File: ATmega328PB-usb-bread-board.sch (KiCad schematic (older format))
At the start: 37 parts, among them J1 Conn_01x17, J2 Conn_01x17, J3 USB_B_Micro, J4 AVR-ISP-6, J5 Grove-I2C-connector, J6 Grove-I2C-connector, J7 Grove-I2C-connector, U1 ATmega328PB-MU, U2 CP2102N-A01-GQFN28, U3 LMV358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

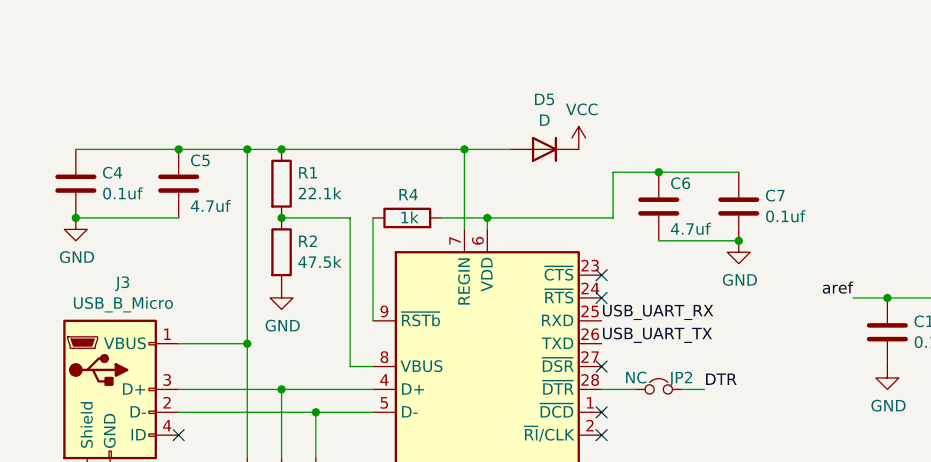
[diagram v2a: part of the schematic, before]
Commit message: Supply 3V3 to cp2102
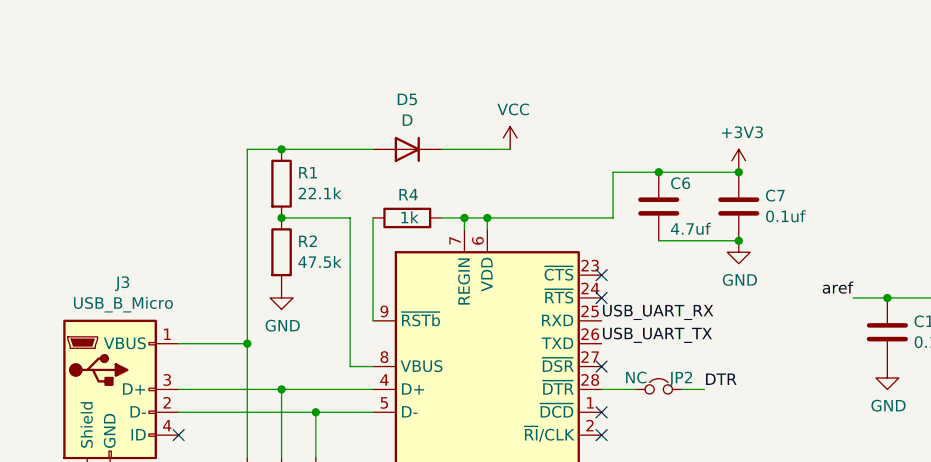
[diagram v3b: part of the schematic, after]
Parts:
- removed C4: 0.1uf, Capacitor_SMD:C_0603_1608Metric, symbol Device:C
- removed C5: 4.7uf, Capacitor_SMD:C_0402_1005Metric, symbol Device:C
- JP1, JP2, JP3, JP4: footprint Jumper:SolderJumper-2_P1.3mm_Bridged_RoundedPad1.0x1.5mm -> my-kicad-footprints:SolderJumper-2_P1.3mm_Bridged_RoundedPad1.0x1.5mm
- U5: footprint (none) -> Package_TO_SOT_SMD:SOT-23-5
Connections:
- net +3V3: now also C6.1, C7.1, R4.2, U2.6 (VDD), U2.7 (REGIN)
- net at D1.1 (K), D5.2 (A), J3.1 (VBUS)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: no longer U2.7 (REGIN)
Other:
- moved on the sheet: D5
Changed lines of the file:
@@
 F 0 "JP1" H 5650 1712 50  0000 C CNN
 F 1 "NC" H 5650 1621 50  0000 C CNN
-F 2 "Jumper:SolderJumper-2_P1.3mm_Bridged_RoundedPad1.0x1.5mm" H 5650 1500 50  0001 C CNN
+F 2 "my-kicad-footprints:SolderJumper-2_P1.3mm_Bridged_RoundedPad1.0x1.5mm" H 5650 1500 50  0001 C CNN
 F 3 "~" H 5650 1500 50  0001 C CNN
 	1    5650 1500
@@
 	1900 1400 2050 1400
 Connection ~ 1900 2250
-Wire Wire Line
-	2050 1400 2850 1400
-Wire Wire Line
-	2850 1400 2850 1750
-Connection ~ 2050 1400
 Connection ~ 2050 1700
 Wire Wire Line
@@
 F 0 "JP4" H 6600 3900 50  0000 C CNN
 F 1 "NC" H 6400 3900 50  0000 C CNN
-F 2 "Jumper:SolderJumper-2_P1.3mm_Bridged_RoundedPad1.0x1.5mm" H 6500 3850 50  0001 C CNN
+F 2 "my-kicad-footprints:SolderJumper-2_P1.3mm_Bridged_RoundedPad1.0x1.5mm" H 6500 3850 50  0001 C CNN
 F 3 "~" H 6500 3850 50  0001 C CNN
 	1    6500 3850
@@
 F 0 "JP3" H 6600 3800 50  0000 C CNN
 F 1 "NC" H 6400 3800 50  0000 C CNN
-F 2 "Jumper:SolderJumper-2_P1.3mm_Bridged_RoundedPad1.0x1.5mm" H 6500 3750 50  0001 C CNN
+F 2 "my-kicad-footprints:SolderJumper-2_P1.3mm_Bridged_RoundedPad1.0x1.5mm" H 6500 3750 50  0001 C CNN
 F 3 "~" H 6500 3750 50  0001 C CNN
 	1    6500 3750
@@
 F 0 "JP2" H 3800 2500 50  0000 C CNN
 F 1 "NC" H 3600 2500 50  0000 C CNN
-F 2 "Jumper:SolderJumper-2_P1.3mm_Bridged_RoundedPad1.0x1.5mm" H 3700 2450 50  0001 C CNN
+F 2 "my-kicad-footprints:SolderJumper-2_P1.3mm_Bridged_RoundedPad1.0x1.5mm" H 3700 2450 50  0001 C CNN
 F 3 "~" H 3700 2450 50  0001 C CNN
 	1    3700 2450
@@
 L Device:D D5
 U 1 1 5F87D197
-P 3200 1400
-F 0 "D5" H 3200 1183 50  0000 C CNN
-F 1 "D" H 3200 1274 50  0000 C CNN
-F 2 "Diode_SMD:D_SOD-123F" H 3200 1400 50  0001 C CNN
-F 3 "~" H 3200 1400 50  0001 C CNN
-	1    3200 1400
+P 2600 1400
+F 0 "D5" H 2600 1183 50  0000 C CNN
+F 1 "D" H 2600 1274 50  0000 C CNN
+F 2 "Diode_SMD:D_SOD-123F" H 2600 1400 50  0001 C CNN
+F 3 "~" H 2600 1400 50  0001 C CNN
+	1    2600 1400
 	-1   0    0    1
 $EndComp
@@
 L power:VCC #PWR0123
 U 1 1 5F87D6DB
-P 3350 1400
-F 0 "#PWR0123" H 3350 1250 50  0001 C CNN
-F 1 "VCC" H 3365 1573 50  0000 C CNN
-F 2 "" H 3350 1400 50  0001 C CNN
-F 3 "" H 3350 1400 50  0001 C CNN
-	1    3350 1400
-	1    0    0    -1
-$EndComp
-Connection ~ 2850 1400
-$Comp
-L my-kicad-symbols:NJM12888F33 U4
-U 1 1 5F8C64C1
-P 9850 1800
-F 0 "U4" H 10000 2250 50  0000 C CNN
-F 1 "NJM12888F33" H 10150 2100 50  0000 C CNN
-F 2 "Package_TO_SOT_SMD:SOT-23-5" H 9850 1800 50  0001 C CNN
-F 3 "" H 9850 1800 50  0001 C CNN
-	1    9850 1800
-	1    0    0    -1
-$EndComp
-$Comp
-L power:VCC #PWR0111
-U 1 1 5F8C761A
-P 9200 1500
-F 0 "#PWR0111" H 9200 1350 50  0001 C CNN
-F 1 "VCC" H 9215 1673 50  0000 C CNN
-F 2 "" H 9200 1500 50  0001 C CNN
-F 3 "" H 9200 1500 50  0001 C CNN
-	1    9200 1500
-	1    0    0    -1
-$EndComp
-$Comp
-L power:GND #PWR0124
-U 1 1 5F8C7AD0
-P 9200 2200
-F 0 "#PWR0124" H 9200 1950 50  0001 C CNN
-F 1 "GND" H 9205 2027 50  0000 C CNN
-F 2 "" H 9200 2200 50  0001 C CNN
-F 3 "" H 9200 2200 50  0001 C CNN
-	1    9200 2200
-	1    0    0    -1
-$EndComp
-$Comp
-L Device:C C8
-U 1 1 5F8C87B4
-P 9200 1800
-F 0 "C8" H 9250 1900 50  0000 L CNN
-F 1 "0.1uf" H 9250 1650 50  0000 L CNN
-F 2 "Capacitor_SMD:C_0603_1608Metric" H 9238 1650 50  0001 C CNN
-F 3 "~" H 9200 1800 50  0001 C CNN
-	1    9200 1800
-	1    0    0    -1
-$EndComp
-Wire Wire Line
-	9200 1500 9450 1500
-Wire Wire Line
-	9450 1500 9450 1800
-Connection ~ 9450 1500
-Wire Wire Line
-	9450 1500 9850 1500
-Wire Wire Line
-	9200 1650 9200 1500
-Connection ~ 9200 1500
-$Comp
-L Device:C C10
-U 1 1 5F8D0B51
-P 10250 2050
-F 0 "C10" H 10300 2150 50  0000 L CNN
-F 1 "10nf" H 10300 1950 50  0000 L CNN
-F 2 "Capacitor_SMD:C_0603_1608Metric" H 10288 1900 50  0001 C CNN
-F 3 "~" H 10250 2050 50  0001 C CNN
-	1    10250 2050
-	1    0    0    -1
-$EndComp
-Wire Wire Line
-	9200 1950 9200 2200
-Wire Wire Line
-	9200 2200 9850 2200
-Connection ~ 9200 2200
-Wire Wire Line
-	9850 2200 9850 2100
-Connection ~ 9850 2200
-Wire Wire Line
-	9850 2200 10250 2200
-$Comp
-L Device:C C12
-U 1 1 5F8D5F68
-P 10600 1950
-F 0 "C12" H 10650 2050 50  0000 L CNN
-F 1 "4.7uf" H 10650 1850 50  0000 L CNN
-F 2 "Capacitor_SMD:C_0402_1005Metric" H 10638 1800 50  0001 C CNN
-F 3 "~" H 10600 1950 50  0001 C CNN
-	1    10600 1950
-	1    0    0    -1
-$EndComp
-$Comp
-L power:+3V3 #PWR0125
-U 1 1 5F8D6BD8
-P 10600 1700
-F 0 "#PWR0125" H 10600 1550 50  0001 C CNN
-F 1 "+3V3" H 10615 1873 50  0000 C CNN
-F 2 "" H 10600 1700 50  0001 C CNN
-F 3 "" H 10600 1700 50  0001 C CNN
-	1    10600 1700
-	1    0    0    -1
-$EndComp
-Wire Wire Line
-	10600 1700 10600 1800
-Wire Wire Line
-	10600 1700 10250 1700
-Connection ~ 10600 1700
-Wire Wire Line
-	10250 2200 10600 2200
-Wire Wire Line
-	10600 2200 10600 2100
-Connection ~ 10250 2200
+P 3050 1400
+F 0 "#PWR0123" H 3050 1250 50  0001 C CNN
+F 1 "VCC" H 3065 1573 50  0000 C CNN
+F 2 "" H 3050 1400 50  0001 C CNN
+F 3 "" H 3050 1400 50  0001 C CNN
+	1    3050 1400
+	1    0    0    -1
+$EndComp
 $Comp
 L power:+3V3 #PWR0126
@@
 F 0 "U5" H 9950 3950 50  0000 L CNN
 F 1 "SiT2001B-MEMS-Clock-Generator" H 9600 3850 50  0000 L CNN
-F 2 "" H 10000 3350 50  0001 C CNN
+F 2 "Package_TO_SOT_SMD:SOT-23-5" H 10000 3350 50  0001 C CNN
 F 3 "" H 10000 3350 50  0001 C CNN
 	1    10000 3350
@@
 16MHz
 NoConn ~ 9600 3350
-Wire Wire Line
-	2850 1400 3050 1400
 $Comp
 L Device:R R4
@@
 	2450 1700 2450 2150
 Wire Wire Line
-	2750 1700 2950 1700
+	2750 1700 2850 1700
 Wire Wire Line
 	2950 1700 2950 1750
-$Comp
-L Device:C C5
-U 1 1 5F8FC33B
-P 1600 1550
-F 0 "C5" H 1650 1650 50  0000 L CNN
-F 1 "4.7uf" H 1650 1450 50  0000 L CNN
-F 2 "Capacitor_SMD:C_0402_1005Metric" H 1638 1400 50  0001 C CNN
-F 3 "~" H 1600 1550 50  0001 C CNN
-	1    1600 1550
-	1    0    0    -1
-$EndComp
-$Comp
-L Device:C C4
-U 1 1 5F9005EE
-P 1150 1550
-F 0 "C4" H 1265 1596 50  0000 L CNN
-F 1 "0.1uf" H 1265 1505 50  0000 L CNN
-F 2 "Capacitor_SMD:C_0603_1608Metric" H 1188 1400 50  0001 C CNN
-F 3 "~" H 1150 1550 50  0001 C CNN
-	1    1150 1550
-	1    0    0    -1
-$EndComp
-$Comp
-L power:GND #PWR0129
-U 1 1 5F9017BB
-P 1150 1700
-F 0 "#PWR0129" H 1150 1450 50  0001 C CNN
-F 1 "GND" H 1155 1527 50  0000 C CNN
-F 2 "" H 1150 1700 50  0001 C CNN
-F 3 "" H 1150 1700 50  0001 C CNN
-	1    1150 1700
-	1    0    0    -1
-$EndComp
-Wire Wire Line
-	1150 1700 1600 1700
-Connection ~ 1150 1700
-Wire Wire Line
-	1900 1400 1600 1400
-Connection ~ 1900 1400
-Connection ~ 1600 1400
-Wire Wire Line
-	1600 1400 1150 1400
 $Comp
 L Device:C C6
@@
 Wire Wire Line
 	3700 1500 4050 1500
+Wire Wire Line
+	2050 1400 2450 1400
+Connection ~ 2050 1400
+$Comp
+L power:+3V3 #PWR?
+U 1 1 5F92FD3C
+P 4050 1500
+F 0 "#PWR?" H 4050 1350 50  0001 C CNN
+F 1 "+3V3" H 4065 1673 50  0000 C CNN
+F 2 "" H 4050 1500 50  0001 C CNN
+F 3 "" H 4050 1500 50  0001 C CNN
+	1    4050 1500
+	1    0    0    -1
+$EndComp
+Connection ~ 4050 1500
+Wire Wire Line
+	10600 2200 10600 2100
+Wire Wire Line
+	10600 1700 10250 1700
+Wire Wire Line
+	10600 1700 10600 1800
+Connection ~ 10600 1700
+$Comp
+L power:+3V3 #PWR0125
+U 1 1 5F8D6BD8
+P 10600 1700
+F 0 "#PWR0125" H 10600 1550 50  0001 C CNN
+F 1 "+3V3" H 10615 1873 50  0000 C CNN
+F 2 "" H 10600 1700 50  0001 C CNN
+F 3 "" H 10600 1700 50  0001 C CNN
+	1    10600 1700
+	1    0    0    -1
+$EndComp
+$Comp
+L Device:C C12
+U 1 1 5F8D5F68
+P 10600 1950
+F 0 "C12" H 10650 2050 50  0000 L CNN
+F 1 "4.7uf" H 10650 1850 50  0000 L CNN
+F 2 "Capacitor_SMD:C_0402_1005Metric" H 10638 1800 50  0001 C CNN
+F 3 "~" H 10600 1950 50  0001 C CNN
+	1    10600 1950
+	1    0    0    -1
+$EndComp
+Wire Wire Line
+	9850 2200 9850 2100
+Connection ~ 9850 2200
+Wire Wire Line
+	9200 2200 9850 2200
+Wire Wire Line
+	9200 1950 9200 2200
+Wire Wire Line
+	10250 2200 10600 2200
+Wire Wire Line
+	9850 2200 10250 2200
+Connection ~ 10250 2200
+$Comp
+L Device:C C10
+U 1 1 5F8D0B51
+P 10250 2050
+F 0 "C10" H 10300 2150 50  0000 L CNN
+F 1 "10nf" H 10300 1950 50  0000 L CNN
+F 2 "Capacitor_SMD:C_0603_1608Metric" H 10288 1900 50  0001 C CNN
+F 3 "~" H 10250 2050 50  0001 C CNN
+	1    10250 2050
+	1    0    0    -1
+$EndComp
+Wire Wire Line
+	9200 1650 9200 1500
+Wire Wire Line
+	9450 1500 9850 1500
+Wire Wire Line
+	9450 1500 9450 1800
+Connection ~ 9450 1500
+Wire Wire Line
+	9200 1500 9450 1500
+$Comp
+L Device:C C8
+U 1 1 5F8C87B4
+P 9200 1800
+F 0 "C8" H 9250 1900 50  0000 L CNN
+F 1 "0.1uf" H 9250 1650 50  0000 L CNN
+F 2 "Capacitor_SMD:C_0603_1608Metric" H 9238 1650 50  0001 C CNN
+F 3 "~" H 9200 1800 50  0001 C CNN
+	1    9200 1800
+	1    0    0    -1
+$EndComp
+Connection ~ 9200 2200
+$Comp
+L power:GND #PWR0124
+U 1 1 5F8C7AD0
+P 9200 2200
+F 0 "#PWR0124" H 9200 1950 50  0001 C CNN
+F 1 "GND" H 9205 2027 50  0000 C CNN
+F 2 "" H 9200 2200 50  0001 C CNN
+F 3 "" H 9200 2200 50  0001 C CNN
+	1    9200 2200
+	1    0    0    -1
+$EndComp
+Connection ~ 9200 1500
+$Comp
+L power:VCC #PWR0111
+U 1 1 5F8C761A
+P 9200 1500
+F 0 "#PWR0111" H 9200 1350 50  0001 C CNN
+F 1 "VCC" H 9215 1673 50  0000 C CNN
+F 2 "" H 9200 1500 50  0001 C CNN
+F 3 "" H 9200 1500 50  0001 C CNN
+	1    9200 1500
+	1    0    0    -1
+$EndComp
+$Comp
+L my-kicad-symbols:NJM12888F33 U4
+U 1 1 5F8C64C1
+P 9850 1800
+F 0 "U4" H 10000 2250 50  0000 C CNN
+F 1 "NJM12888F33" H 10150 2100 50  0000 C CNN
+F 2 "Package_TO_SOT_SMD:SOT-23-5" H 9850 1800 50  0001 C CNN
+F 3 "" H 9850 1800 50  0001 C CNN
+	1    9850 1800
+	1    0    0    -1
+$EndComp
+Wire Wire Line
+	2750 1400 3050 1400
+Wire Wire Line
+	2850 1700 2850 1750
+Connection ~ 2850 1700
+Wire Wire Line
+	2850 1700 2950 1700
 $EndSCHEMATC

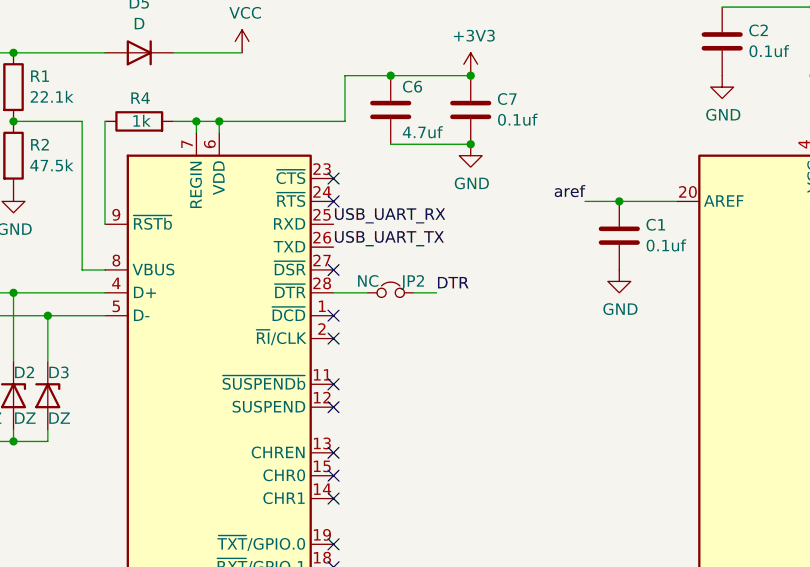
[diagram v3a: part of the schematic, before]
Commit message: Remove jumper for DTR
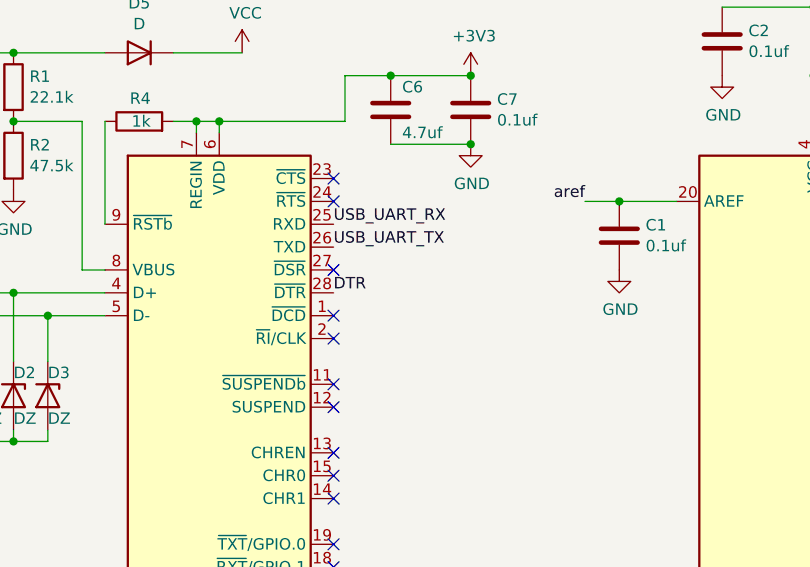
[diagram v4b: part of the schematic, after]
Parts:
- removed JP2: NC, my-kicad-footprints:SolderJumper-2_P1.3mm_Bridged_RoundedPad1.0x1.5mm, symbol ATmega328PB-usb-bread-board-rescue:Jumper_NC_Small-Device
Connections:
- net DTR: now also U2.28 (~DTR)
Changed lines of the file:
@@
 Text Label 7950 2800 0    50   ~ 0
 DTR
-Text Label 3900 2450 0    50   ~ 0
-DTR
-$Comp
-L ATmega328PB-usb-bread-board-rescue:Jumper_NC_Small-Device JP2
-U 1 1 5F5F147B
-P 3700 2450
-F 0 "JP2" H 3800 2500 50  0000 C CNN
-F 1 "NC" H 3600 2500 50  0000 C CNN
-F 2 "my-kicad-footprints:SolderJumper-2_P1.3mm_Bridged_RoundedPad1.0x1.5mm" H 3700 2450 50  0001 C CNN
-F 3 "~" H 3700 2450 50  0001 C CNN
-	1    3700 2450
-	1    0    0    -1
-$EndComp
-Wire Wire Line
-	3600 2450 3450 2450
-Wire Wire Line
-	3800 2450 3900 2450
 NoConn ~ 1600 2650
 $Comp
@@
 Connection ~ 2050 1400
 $Comp
-L power:+3V3 #PWR?
+L power:+3V3 #PWR0129
 U 1 1 5F92FD3C
 P 4050 1500
-F 0 "#PWR?" H 4050 1350 50  0001 C CNN
+F 0 "#PWR0129" H 4050 1350 50  0001 C CNN
 F 1 "+3V3" H 4065 1673 50  0000 C CNN
 F 2 "" H 4050 1500 50  0001 C CNN
@@
 Wire Wire Line
 	2850 1700 2950 1700
+Text Label 3450 2450 0    50   ~ 0
+DTR
 $EndSCHEMATC
